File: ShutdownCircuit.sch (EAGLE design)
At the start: 26 parts

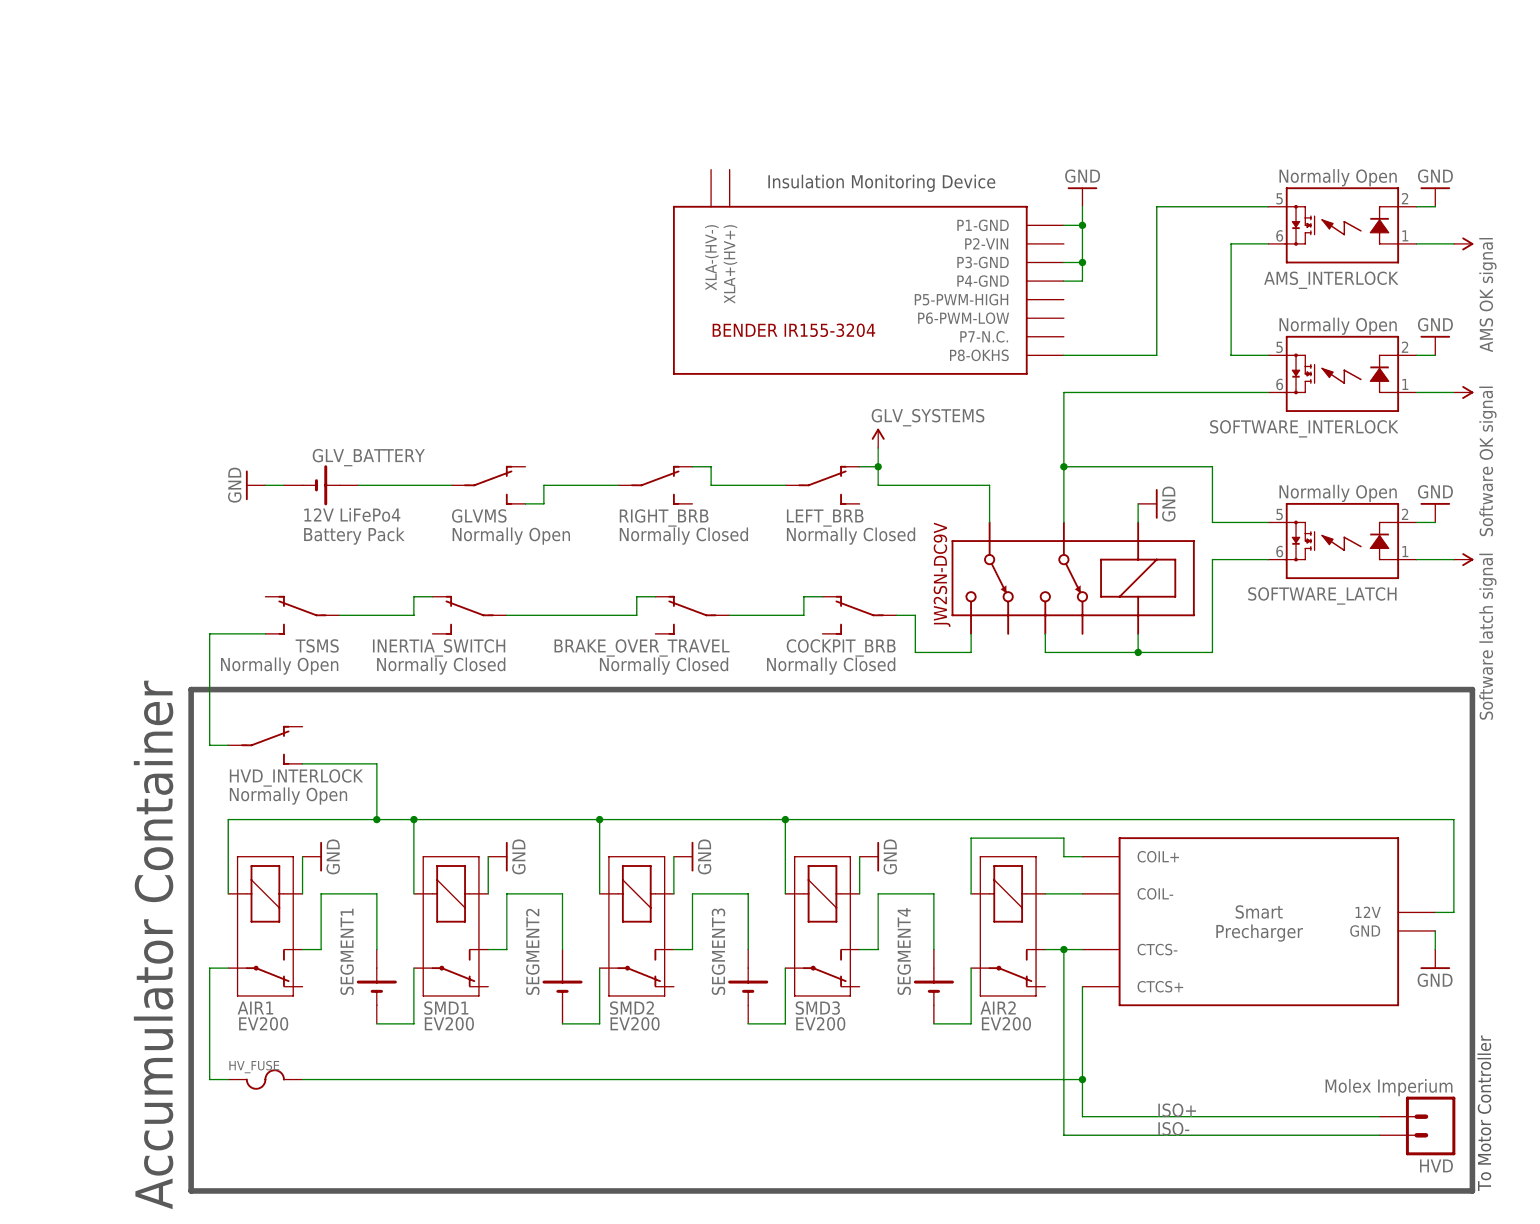
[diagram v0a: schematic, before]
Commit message: Document connections on shutdown circuit
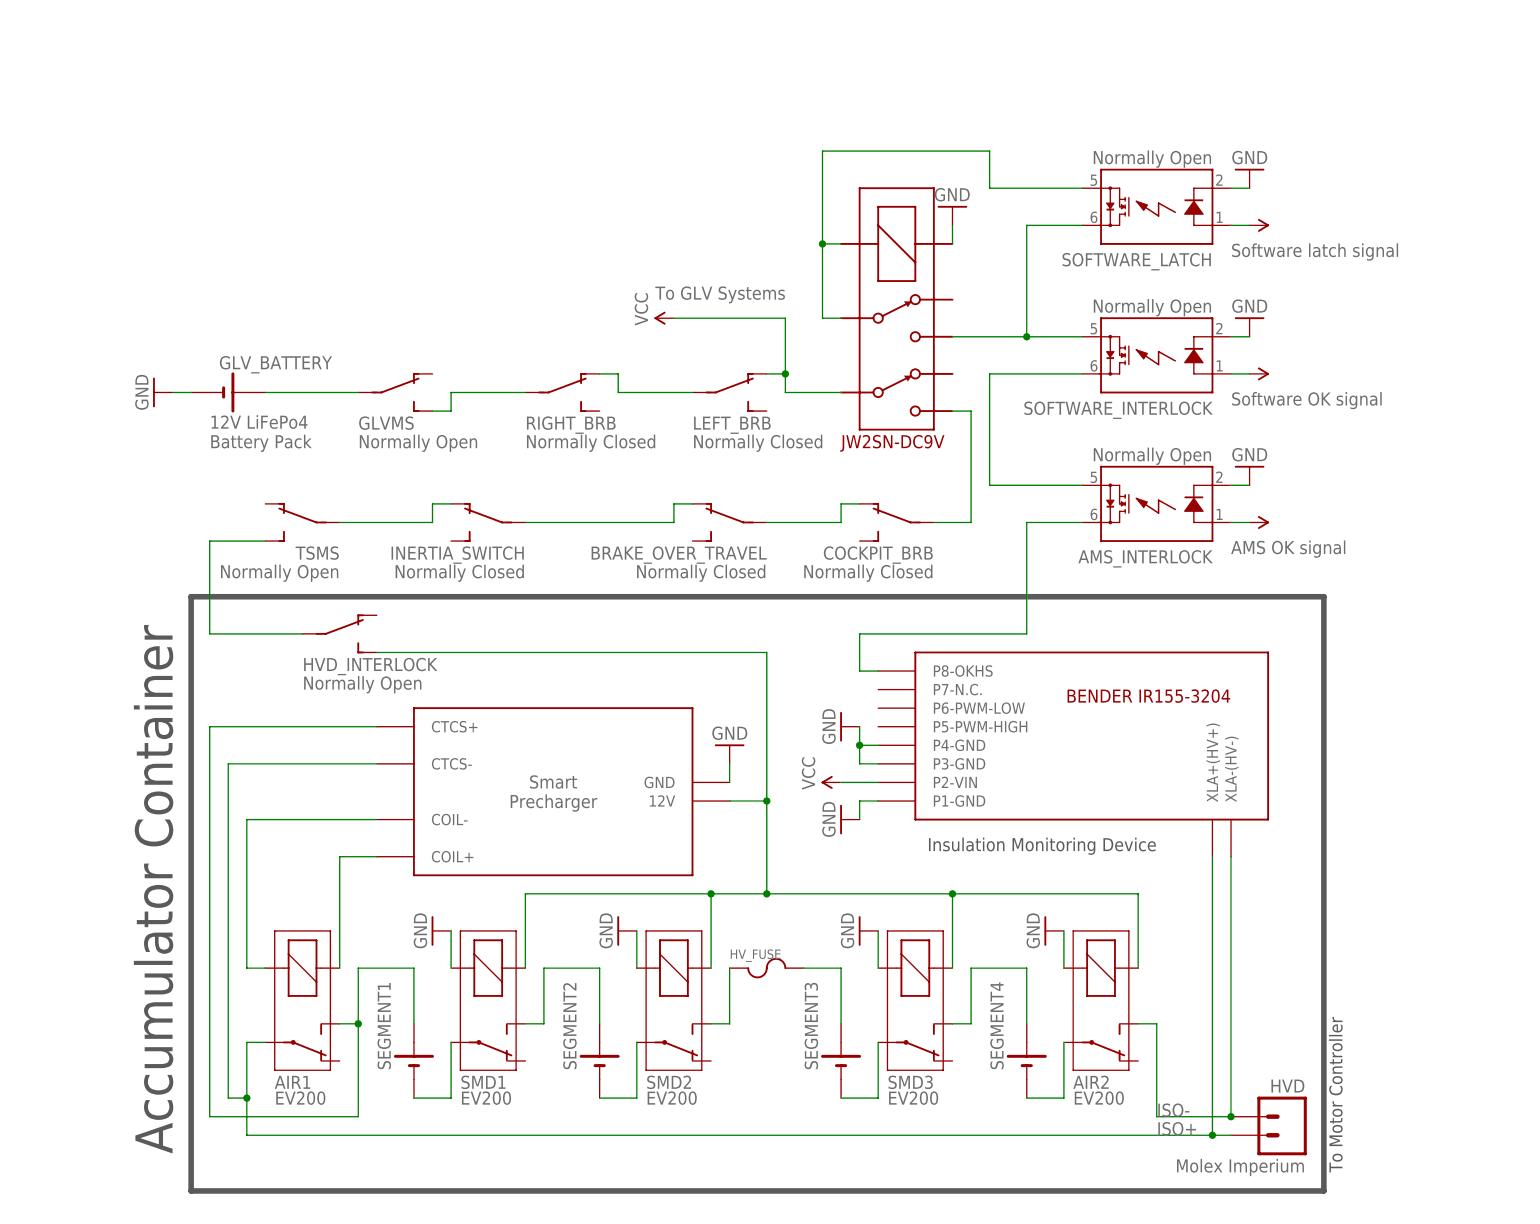
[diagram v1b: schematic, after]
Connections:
- removed net N$45: AIR1.S, SEGMENT1.+
- removed net N$58: AIR2.2, U$3.COIL+
- removed net N$60: AIR2.1, U$3.COIL-
- removed net N$7: SOFTWARE_LATCH.IO1, U$1.4, U$1.COIL+
- new net N$18: AIR1.2, U$3.COIL-
- new net N$19: AIR1.1, U$3.COIL+
- new net N$20: HV_FUSE.1, SMD2.S
- new net N$22: AIR1.S, SEGMENT1.+, U$3.CTCS+
- net GND: now also AIR2.2, SMD1.2, SMD2.2, SMD3.2, U$1.COIL+; no longer AIR1.1, SMD1.1, SMD2.1, SMD3.1, U$1.COIL-
- net ISO+: now also AIR1.P, U$2.XLA+(HV+), U$3.CTCS-; no longer HV_FUSE.2, U$3.CTCS+
- net ISO-: now also U$2.XLA-(HV-); no longer U$3.CTCS-
- net N$15: now also HV_FUSE.2; no longer SMD2.S
- net N$16: now also AMS_INTERLOCK.IO1, U$2.P8-OKHS; no longer AIR1.P, HV_FUSE.1
- net N$4: now also SOFTWARE_INTERLOCK.IO2, SOFTWARE_LATCH.IO1, U$1.4; no longer AMS_INTERLOCK.IO2, U$2.P8-OKHS
- net N$5: now also AMS_INTERLOCK.IO2, SOFTWARE_INTERLOCK.IO1; no longer AMS_INTERLOCK.IO1, SOFTWARE_INTERLOCK.IO2
- net N$6: now also U$1.COIL-; no longer SOFTWARE_INTERLOCK.IO1
- net SHUTDOWN_CIRCUIT: now also AIR2.1, SMD1.1, SMD2.1, SMD3.1; no longer AIR1.2, SMD1.2, SMD2.2, SMD3.2
- net VIN: now also U$2.P2-VIN
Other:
- note added: "AMS OK signal"
- note added: "Software OK signal"
- note added: "Software latch signal"
- note added: "To GLV Systems"
- moved on the sheet: AIR1, AIR2, AMS_INTERLOCK, BRAKE_OVER_TRAVEL, COCKPIT_BRB, GLVMS, GLV_BATTERY, HVD, HVD_INTERLOCK, HV_FUSE, INERTIA_SWITCH, LEFT_BRB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

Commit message: Add software shutoff relay to shutdown circuit
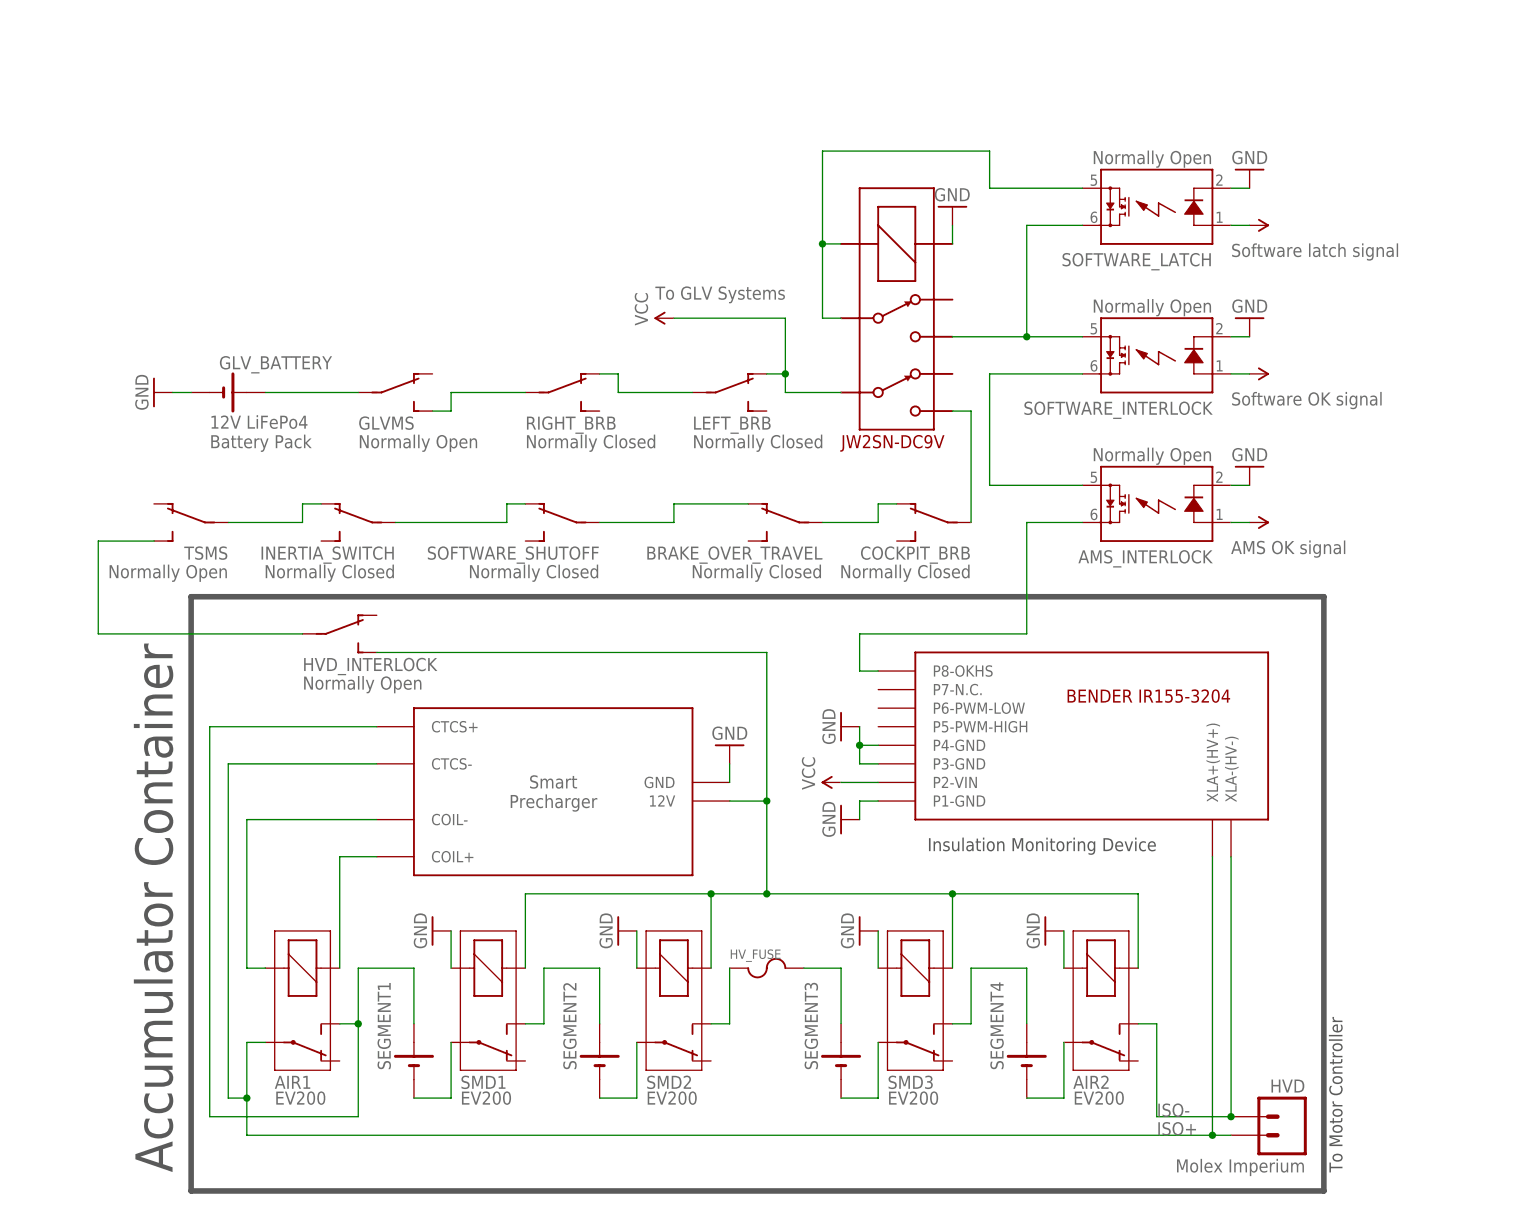
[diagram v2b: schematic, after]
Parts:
- added SOFTWARE_SHUTOFF: Normally Closed, HyTechSymbols:SWITCH_SPST
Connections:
- new net N$7: INERTIA_SWITCH.P, SOFTWARE_SHUTOFF.O
- net N$10: now also SOFTWARE_SHUTOFF.P; no longer INERTIA_SWITCH.P
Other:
- moved on the sheet: BRAKE_OVER_TRAVEL, COCKPIT_BRB, INERTIA_SWITCH, TSMS
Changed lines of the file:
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@@
 <?xml version="1.0" encoding="utf-8"?>
 <!DOCTYPE eagle SYSTEM "eagle.dtd">
-<eagle version="7.6.0">
+<eagle version="7.7.0">
 <drawing>
 <settings>
@@
 <part name="GLV_SYSTEMS1" library="HyTechSymbols" deviceset="VIN" device="" value="VCC"/>
 <part name="GND9" library="HyTechSymbols" deviceset="GND" device=""/>
+<part name="SOFTWARE_SHUTOFF" library="HyTechSymbols" deviceset="SWITCH_SPST" device="" value="Normally Closed"/>
 </parts>
 <sheets>
@@
 <wire x1="154.94" y1="0" x2="0" y2="0" width="0.762" layer="97"/>
 <wire x1="0" y1="0" x2="0" y2="81.28" width="0.762" layer="97"/>
-<text x="-2.54" y="5.08" size="5.08" layer="97" rot="R90">Accumulator Container</text>
+<text x="-2.54" y="2.54" size="5.08" layer="97" rot="R90">Accumulator Container</text>
 <text x="157.48" y="2.54" size="1.778" layer="97" rot="R90">To Motor Controller</text>
 <text x="132.08" y="48.26" size="1.778" layer="97" rot="R180">Insulation Monitoring Device</text>
@@
 <instance part="U$2" gate="G$1" x="147.32" y="73.66" rot="R180"/>
 <instance part="GND2" gate="1" x="88.9" y="50.8" rot="R270"/>
-<instance part="COCKPIT_BRB" gate="SPST" x="96.52" y="91.44" rot="MR270"/>
-<instance part="INERTIA_SWITCH" gate="SPST" x="40.64" y="91.44" rot="MR270"/>
-<instance part="BRAKE_OVER_TRAVEL" gate="SPST" x="73.66" y="91.44" rot="MR270"/>
-<instance part="TSMS" gate="SPST" x="15.24" y="91.44" rot="MR270"/>
+<instance part="COCKPIT_BRB" gate="SPST" x="101.6" y="91.44" rot="MR270"/>
+<instance part="INERTIA_SWITCH" gate="SPST" x="22.86" y="91.44" rot="MR270"/>
+<instance part="BRAKE_OVER_TRAVEL" gate="SPST" x="81.28" y="91.44" rot="MR270"/>
+<instance part="TSMS" gate="SPST" x="0" y="91.44" rot="MR270"/>
 <instance part="HVD_INTERLOCK" gate="SPST" x="20.32" y="76.2" rot="R270"/>
 <instance part="SEGMENT1" gate="G$1" x="30.48" y="17.78" rot="R90"/>
@@
 <instance part="GLV_SYSTEMS1" gate="G$1" x="88.9" y="55.88" rot="R90"/>
 <instance part="GND9" gate="1" x="88.9" y="63.5" rot="R270"/>
+<instance part="SOFTWARE_SHUTOFF" gate="SPST" x="50.8" y="91.44" rot="MR270"/>
 </instances>
 <busses>
@@
 <segment>
 <pinref part="COCKPIT_BRB" gate="SPST" pin="O"/>
-<wire x1="91.44" y1="93.98" x2="88.9" y2="93.98" width="0.1524" layer="91"/>
-<wire x1="88.9" y1="93.98" x2="88.9" y2="91.44" width="0.1524" layer="91"/>
+<wire x1="96.52" y1="93.98" x2="93.98" y2="93.98" width="0.1524" layer="91"/>
+<wire x1="93.98" y1="93.98" x2="93.98" y2="91.44" width="0.1524" layer="91"/>
 <pinref part="BRAKE_OVER_TRAVEL" gate="SPST" pin="P"/>
-<wire x1="88.9" y1="91.44" x2="78.74" y2="91.44" width="0.1524" layer="91"/>
+<wire x1="93.98" y1="91.44" x2="86.36" y2="91.44" width="0.1524" layer="91"/>
 </segment>
 </net>
@@
 <segment>
 <pinref part="BRAKE_OVER_TRAVEL" gate="SPST" pin="O"/>
-<wire x1="68.58" y1="93.98" x2="66.04" y2="93.98" width="0.1524" layer="91"/>
+<wire x1="76.2" y1="93.98" x2="66.04" y2="93.98" width="0.1524" layer="91"/>
 <wire x1="66.04" y1="93.98" x2="66.04" y2="91.44" width="0.1524" layer="91"/>
-<pinref part="INERTIA_SWITCH" gate="SPST" pin="P"/>
-<wire x1="66.04" y1="91.44" x2="45.72" y2="91.44" width="0.1524" layer="91"/>
+<pinref part="SOFTWARE_SHUTOFF" gate="SPST" pin="P"/>
+<wire x1="66.04" y1="91.44" x2="55.88" y2="91.44" width="0.1524" layer="91"/>
 </segment>
 </net>
@@
 <segment>
 <pinref part="INERTIA_SWITCH" gate="SPST" pin="O"/>
-<wire x1="35.56" y1="93.98" x2="33.02" y2="93.98" width="0.1524" layer="91"/>
-<wire x1="33.02" y1="93.98" x2="33.02" y2="91.44" width="0.1524" layer="91"/>
+<wire x1="17.78" y1="93.98" x2="15.24" y2="93.98" width="0.1524" layer="91"/>
+<wire x1="15.24" y1="93.98" x2="15.24" y2="91.44" width="0.1524" layer="91"/>
 <pinref part="TSMS" gate="SPST" pin="P"/>
-<wire x1="33.02" y1="91.44" x2="20.32" y2="91.44" width="0.1524" layer="91"/>
+<wire x1="15.24" y1="91.44" x2="5.08" y2="91.44" width="0.1524" layer="91"/>
 </segment>
 </net>
@@
 <wire x1="104.14" y1="106.68" x2="106.68" y2="106.68" width="0.1524" layer="91"/>
 <wire x1="106.68" y1="106.68" x2="106.68" y2="91.44" width="0.1524" layer="91"/>
-<wire x1="106.68" y1="91.44" x2="101.6" y2="91.44" width="0.1524" layer="91"/>
 </segment>
 </net>
@@
 <segment>
 <pinref part="TSMS" gate="SPST" pin="S"/>
-<wire x1="10.16" y1="88.9" x2="2.54" y2="88.9" width="0.1524" layer="91"/>
-<wire x1="2.54" y1="88.9" x2="2.54" y2="76.2" width="0.1524" layer="91"/>
+<wire x1="-5.08" y1="88.9" x2="-12.7" y2="88.9" width="0.1524" layer="91"/>
+<wire x1="-12.7" y1="88.9" x2="-12.7" y2="76.2" width="0.1524" layer="91"/>
 <pinref part="HVD_INTERLOCK" gate="SPST" pin="P"/>
-<wire x1="2.54" y1="76.2" x2="15.24" y2="76.2" width="0.1524" layer="91"/>
+<wire x1="-12.7" y1="76.2" x2="15.24" y2="76.2" width="0.1524" layer="91"/>
 </segment>
 </net>
@@
 </segment>
 </net>
+<net name="N$7" class="0">
+<segment>
+<pinref part="INERTIA_SWITCH" gate="SPST" pin="P"/>
+<wire x1="27.94" y1="91.44" x2="43.18" y2="91.44" width="0.1524" layer="91"/>
+<wire x1="43.18" y1="91.44" x2="43.18" y2="93.98" width="0.1524" layer="91"/>
+<pinref part="SOFTWARE_SHUTOFF" gate="SPST" pin="O"/>
+<wire x1="43.18" y1="93.98" x2="45.72" y2="93.98" width="0.1524" layer="91"/>
+</segment>
+</net>
